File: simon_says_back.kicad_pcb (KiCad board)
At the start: 2 copper layers, 97 x 60 mm, 4 parts

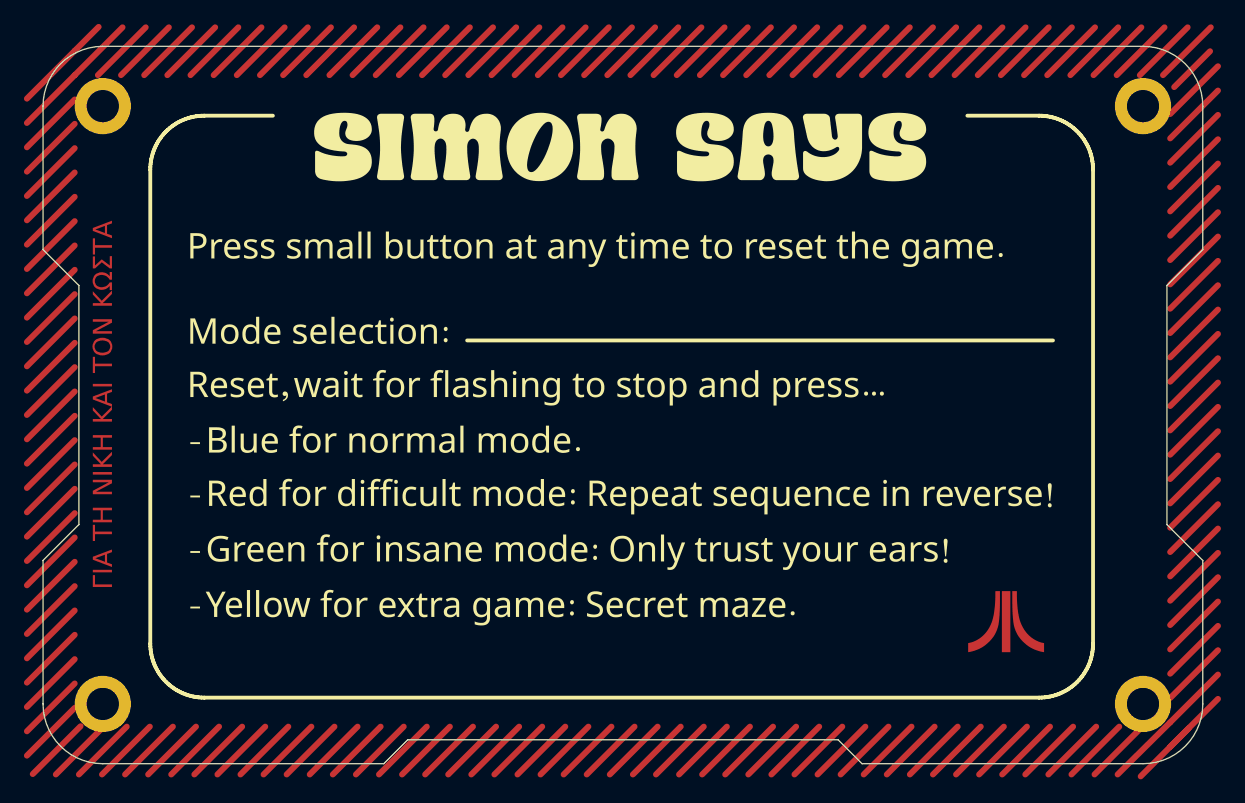
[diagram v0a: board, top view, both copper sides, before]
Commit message: Minor aesthetic changes
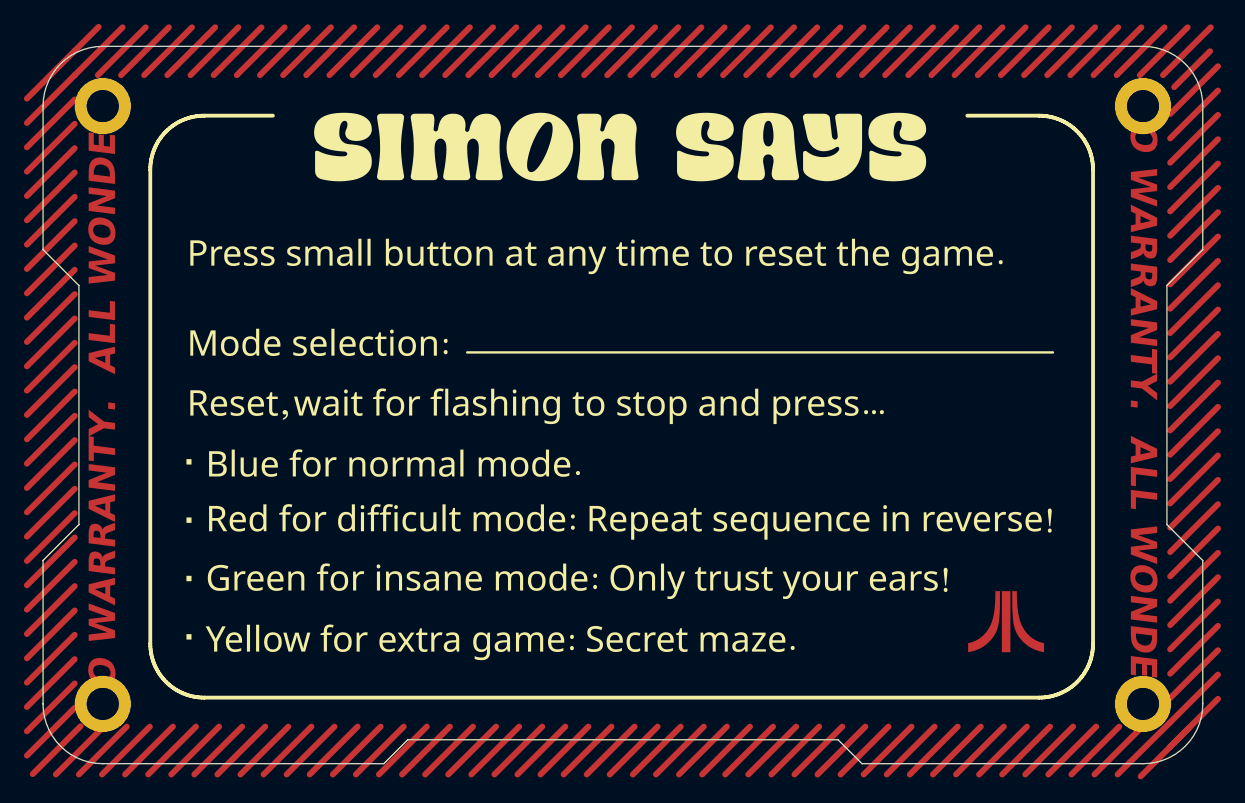
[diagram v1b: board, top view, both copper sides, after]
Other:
- board text added: "."
- board text added: "NO WARRANTY. ALL WONDER."
- board text removed: "JLCJLCJLCJLC"
- board text removed: "ΓΙΑ ΤΗ ΝΙΚΗ ΚΑΙ ΤΟΝ ΚΩΣΤΑ"
